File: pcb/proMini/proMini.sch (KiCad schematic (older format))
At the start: 6 parts

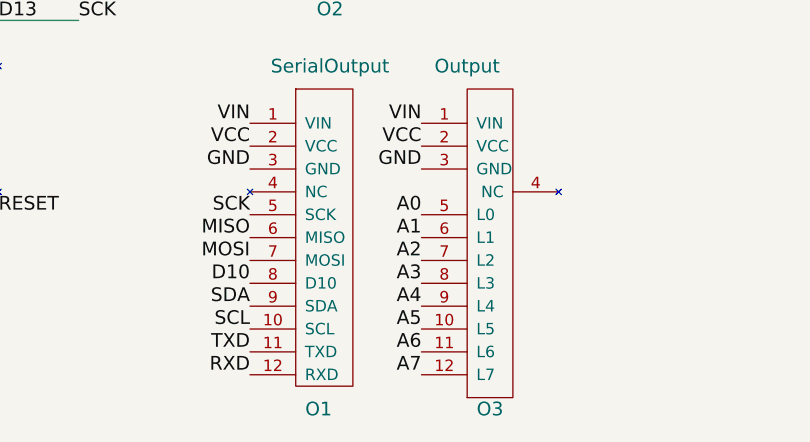
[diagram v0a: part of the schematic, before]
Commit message: Added a Rotary Encoder module. Tidied up a couple of modules before printing them.
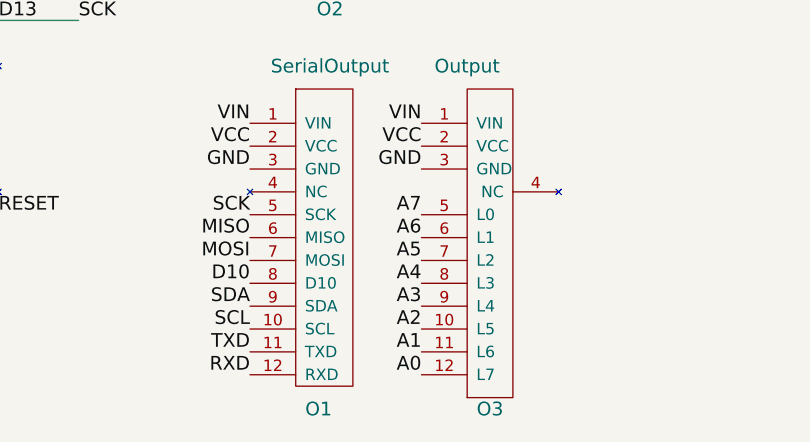
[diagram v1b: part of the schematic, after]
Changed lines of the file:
@@
 Text Label 6050 3400 2    60   ~ 0
 GND
-Text Label 6050 3600 2    60   ~ 0
+Text Label 6050 4300 2    60   ~ 0
 A0
-Text Label 6050 3700 2    60   ~ 0
+Text Label 6050 4200 2    60   ~ 0
 A1
+Text Label 6050 4100 2    60   ~ 0
+A2
+Text Label 6050 4000 2    60   ~ 0
+A3
+Text Label 6050 3900 2    60   ~ 0
+A4
 Text Label 6050 3800 2    60   ~ 0
-A2
-Text Label 6050 3900 2    60   ~ 0
-A3
-Text Label 6050 4000 2    60   ~ 0
-A4
-Text Label 6050 4100 2    60   ~ 0
 A5
 Text Label 4200 1650 0    60   ~ 0
@@
 Text Label 1300 2450 2    60   ~ 0
 SDA
-Text Label 6050 4200 2    60   ~ 0
+Text Label 6050 3700 2    60   ~ 0
 A6
-Text Label 6050 4300 2    60   ~ 0
+Text Label 6050 3600 2    60   ~ 0
 A7
 $Comp
